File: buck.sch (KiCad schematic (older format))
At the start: 12 parts, among them U5 MP1584EN

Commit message: Rename to Sailor Hat
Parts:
- U5: symbol pi-supercap-ups:MP1584EN -> sailor-hat-rescue:MP1584EN-sailor-hat
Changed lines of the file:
@@
-EESchema Schematic File Version 5
-LIBS:pi-supercap-ups-cache
+EESchema Schematic File Version 4
 EELAYER 30 0
 EELAYER END
@@
 Comment3 ""
 Comment4 ""
-Comment5 ""
-Comment6 ""
-Comment7 ""
-Comment8 ""
-Comment9 ""
 $EndDescr
 $Comp
-L pi-supercap-ups:MP1584EN U?
+L sailor-hat-rescue:MP1584EN-sailor-hat U?
 U 1 1 5CA62D44
 P 3050 2350

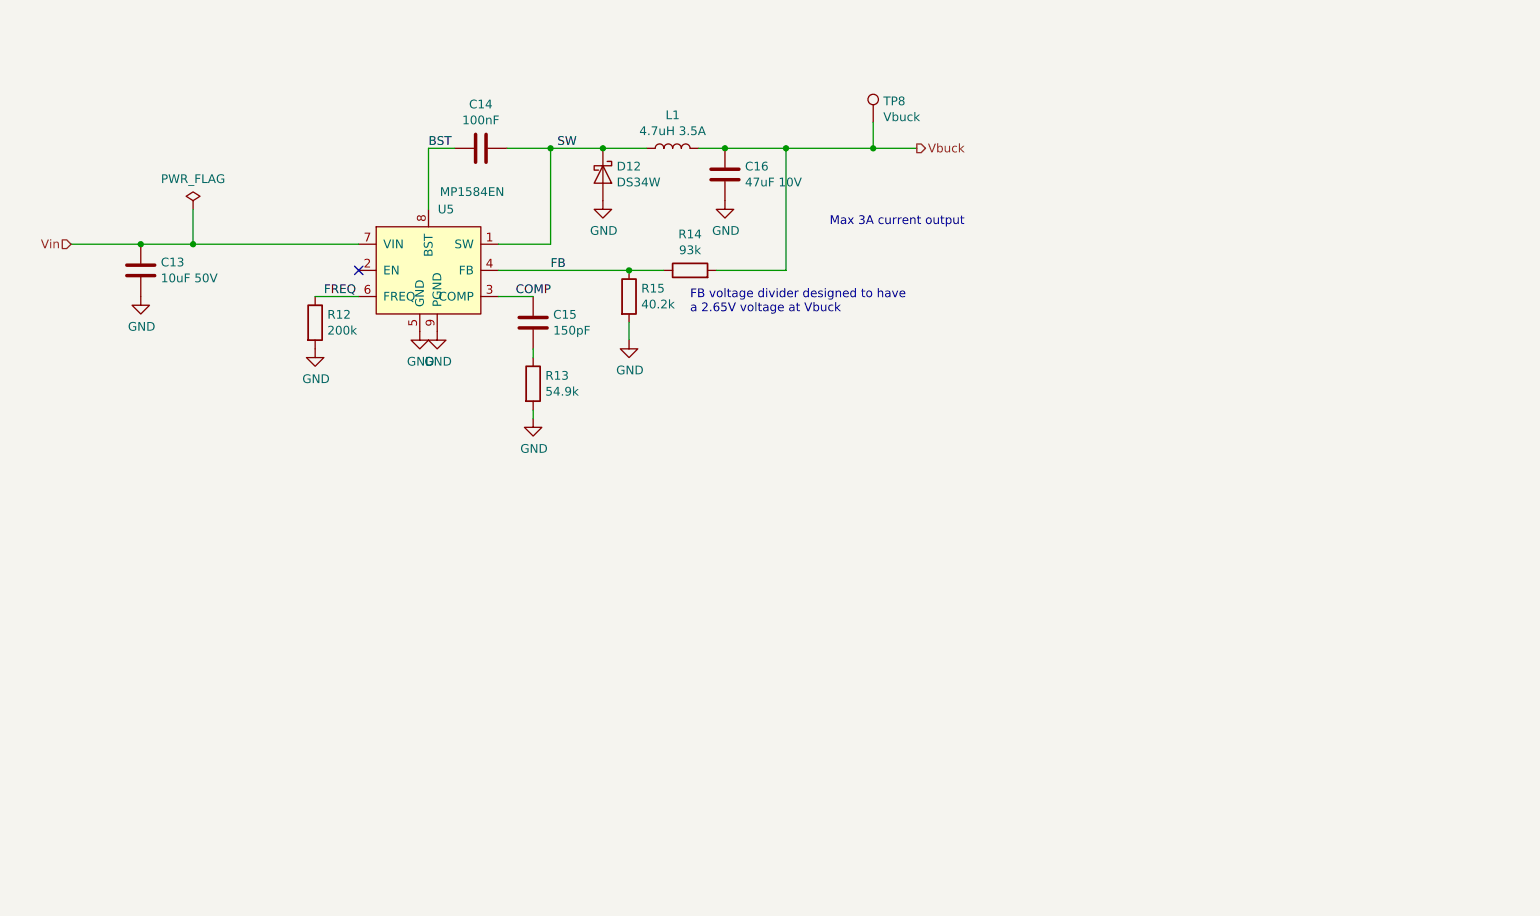
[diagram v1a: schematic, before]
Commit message: Implement better current limiting
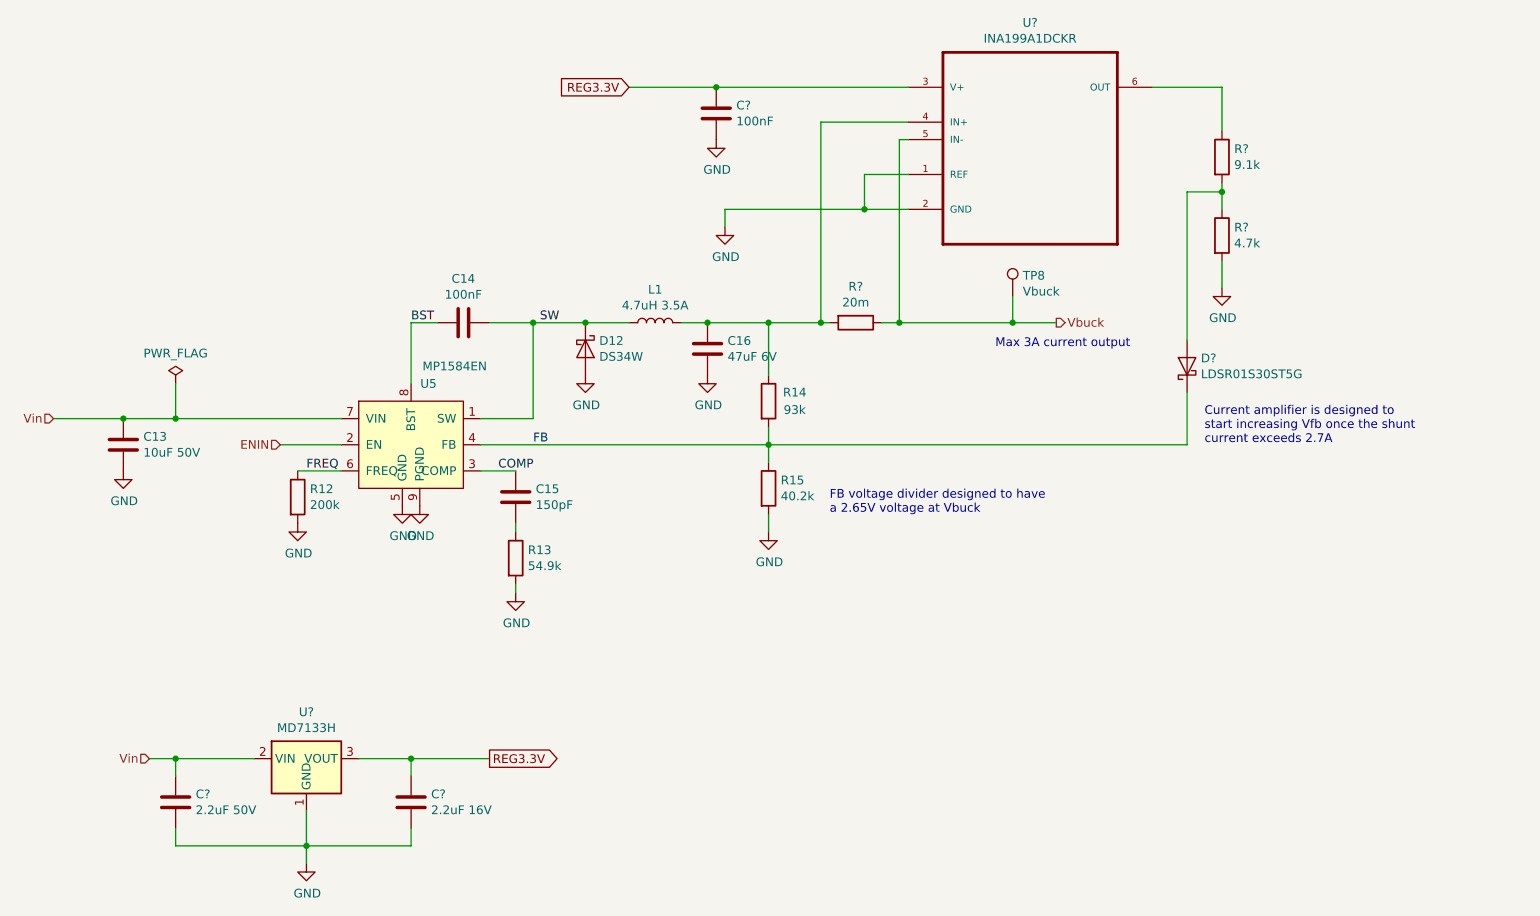
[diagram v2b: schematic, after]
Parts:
- added C?: 100nF, symbol Device:C
- added C?: 2.2uF 50V, symbol Device:C
- added C?: 2.2uF 16V, symbol Device:C
- added D?: LDSR01S30ST5G, symbol Device:D_Schottky
- added R?: 20m, symbol Device:R
- added R?: 9.1k, symbol Device:R
- added R?: 4.7k, symbol Device:R
- added U?: INA199A1DCKR, SOT65P210X110-6N, symbol sailor-hat:INA199A1DCKR
- added U?: MD7133H, Package_TO_SOT_SMD:SOT-89-3, symbol Regulator_Linear:HT75xx-1-SOT89
- C16: value 47uF 10V -> 47uF 6V
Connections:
- net FB: now also R14.2, D?.1 (K); no longer R14.1
- net GND: now also C?.2, C?.2, C?.2, R?.2, U?.1 (GND), U?.1 (REF), U?.2 (GND)
- net Vbuck: now also R?.1, U?.5 (IN-); no longer C16.1, L1.2, R14.2
- net Vin: now also C?.1, U?.2 (VIN)
- net ENIN: now reaches U5.2 (EN)
- new net: C16.1, L1.2, R14.1, R?.2, U?.4 (IN+)
- new net: R?.1, U?.6 (OUT)
- new net: D?.2 (A), R?.1, R?.2
- new net REG3.3V: C?.1, C?.1, U?.3 (V+), U?.3 (VOUT)
- no-connect marks 1 -> 0
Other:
- note added: "Current amplifier is designed to\nstart increasing Vfb once the shunt\ncurrent exceeds 2.7A"
- moved on the sheet: C13, C14, C15, C16, D12, L1, R12, R13, R14, R15, TP8, U5

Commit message: Add test points for new features
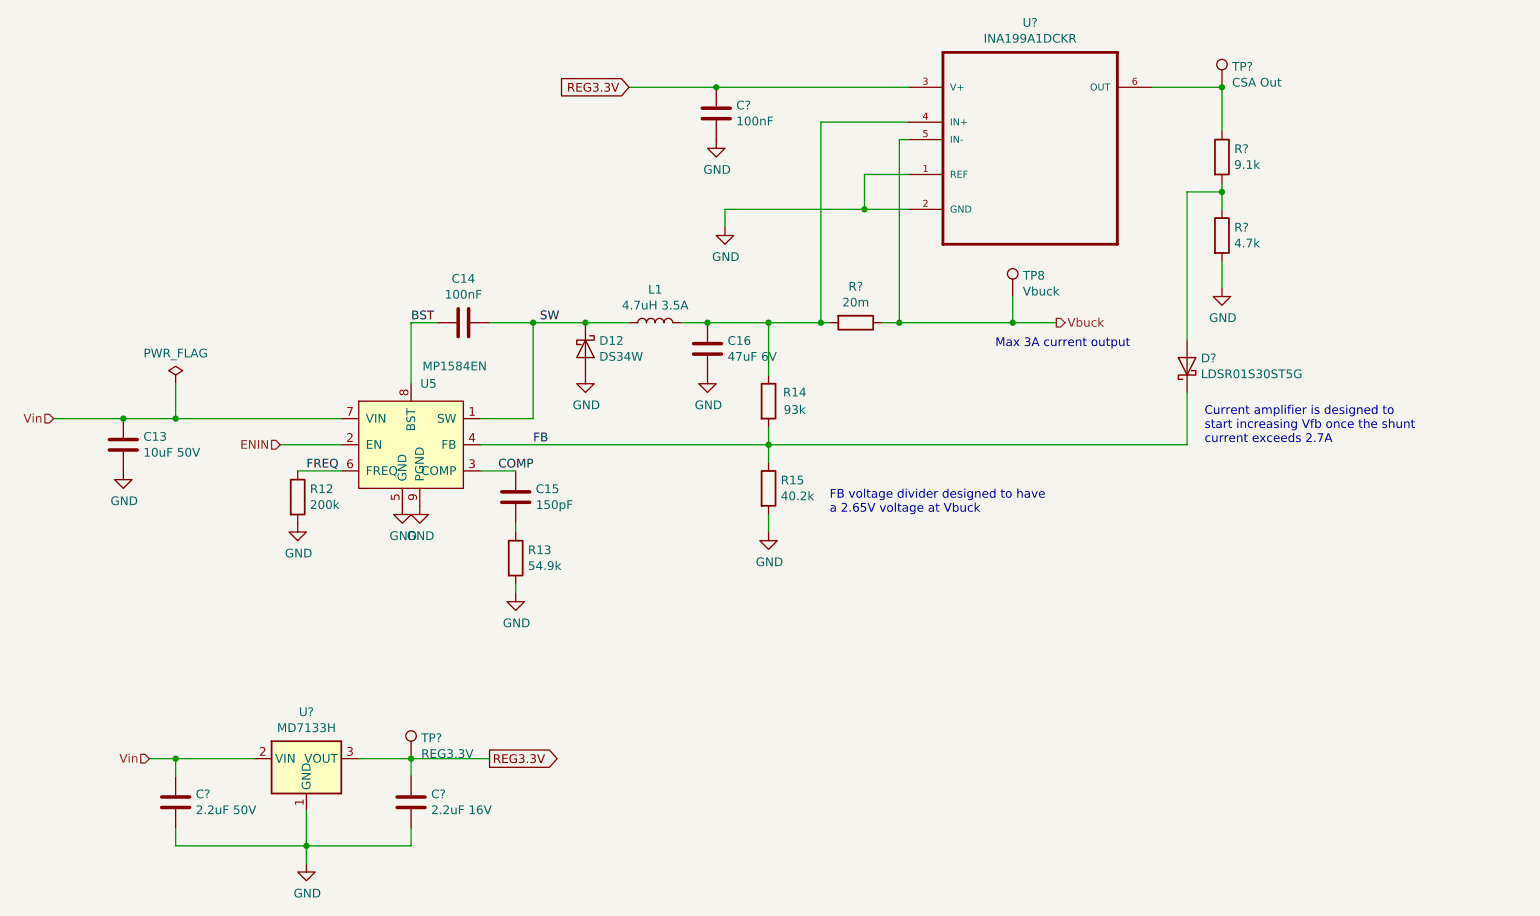
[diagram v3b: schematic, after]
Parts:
- added TP?: CSA Out, symbol Connector:TestPoint
- added TP?: REG3.3V, symbol Connector:TestPoint
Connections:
- net REG3.3V: now also TP?.1
- net at R?.1, U?.6 (OUT): now also TP?.1
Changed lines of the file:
@@
 Wire Wire Line
 	2200 3350 2550 3350
+$Comp
+L Connector:TestPoint TP?
+U 1 1 5E2A7700
+P 7600 1300
+F 0 "TP?" H 7658 1418 50  0000 L CNN
+F 1 "CSA Out" H 7658 1327 50  0000 L CNN
+F 2 "" H 7800 1300 50  0001 C CNN
+F 3 "~" H 7800 1300 50  0001 C CNN
+	1    7600 1300
+	1    0    0    -1
+$EndComp
+Connection ~ 7600 1300
+$Comp
+L Connector:TestPoint TP?
+U 1 1 5E2A8B09
+P 2950 5150
+F 0 "TP?" H 3008 5268 50  0000 L CNN
+F 1 "REG3.3V" H 3008 5177 50  0000 L CNN
+F 2 "" H 3150 5150 50  0001 C CNN
+F 3 "~" H 3150 5150 50  0001 C CNN
+	1    2950 5150
+	1    0    0    -1
+$EndComp
 $EndSCHEMATC

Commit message: Annotate and tweak power flags
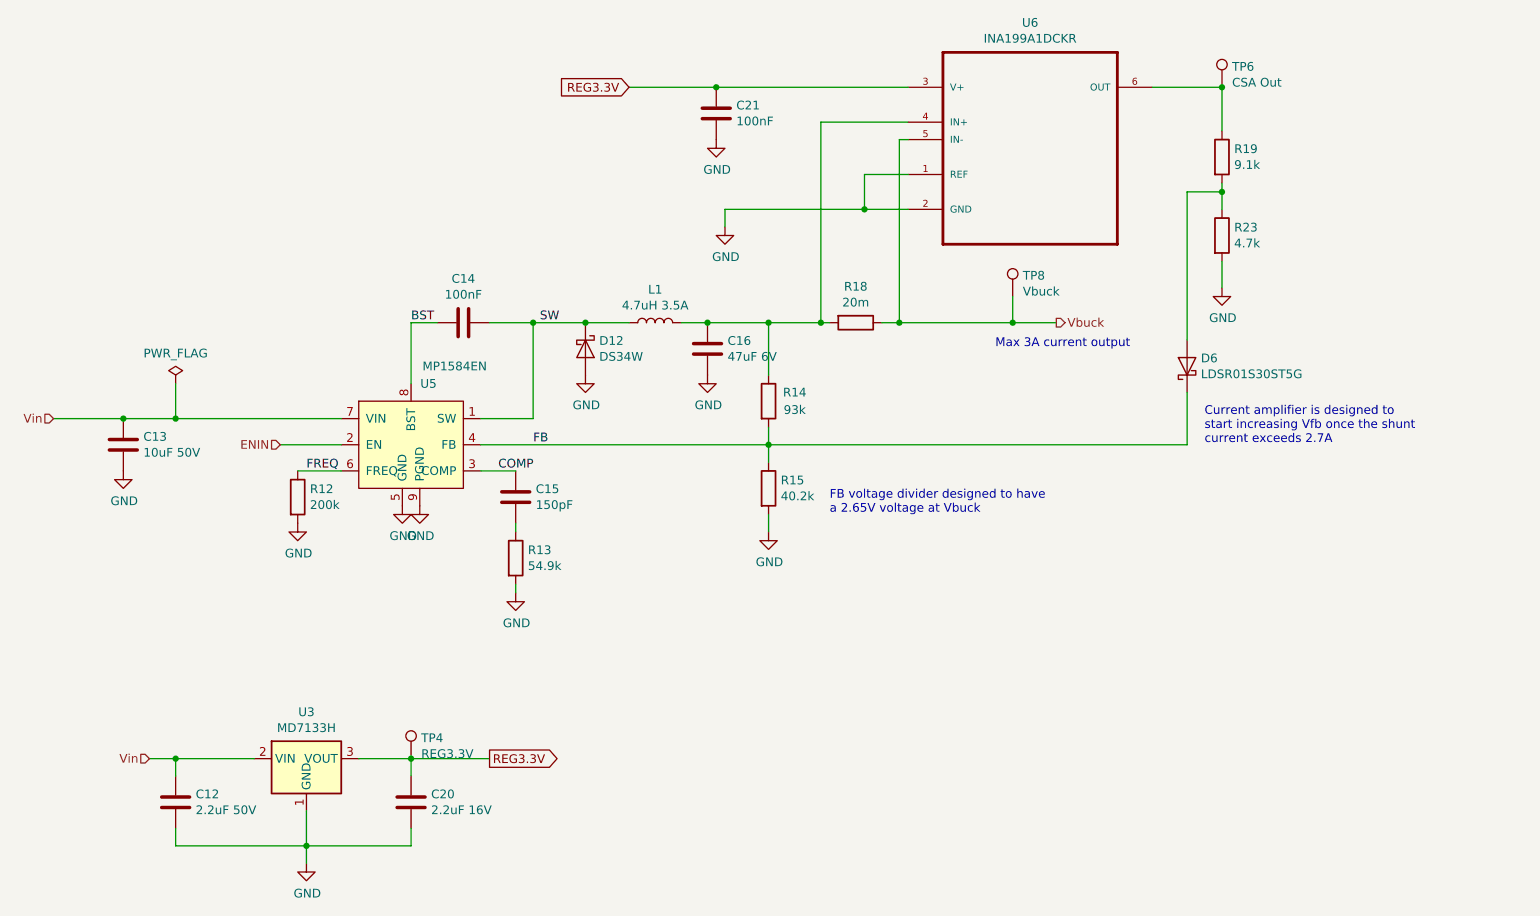
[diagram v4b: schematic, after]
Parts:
- gave numbers to parts that had none: 11
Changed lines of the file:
@@
 Connection ~ 5000 3350
 $Comp
-L sailor-hat:INA199A1DCKR U?
+L sailor-hat:INA199A1DCKR U6
 U 1 1 5E255BE6
 P 6500 1500
-F 0 "U?" H 6500 2070 50  0000 C CNN
+F 0 "U6" H 6500 2070 50  0000 C CNN
 F 1 "INA199A1DCKR" H 6500 1979 50  0000 C CNN
 F 2 "SOT65P210X110-6N" H 6500 1500 50  0001 L BNN
@@
 AR Path="/5E266404" Ref="#PWR?"  Part="1"
 AR Path="/5C3476D8/5E266404" Ref="#PWR?"  Part="1"
-AR Path="/5CA65CC5/5E266404" Ref="#PWR?"  Part="1"
-F 0 "#PWR?" H 4750 1850 50  0001 C CNN
+AR Path="/5CA65CC5/5E266404" Ref="#PWR052"  Part="1"
+F 0 "#PWR052" H 4750 1850 50  0001 C CNN
 F 1 "GND" H 4755 1927 50  0000 C CNN
 F 2 "" H 4750 2100 50  0001 C CNN
@@
 	4750 2000 5550 2000
 $Comp
-L Device:C C?
+L Device:C C21
 U 1 1 5E2673D4
 P 4700 1450
-F 0 "C?" H 4815 1496 50  0000 L CNN
+F 0 "C21" H 4815 1496 50  0000 L CNN
 F 1 "100nF" H 4815 1405 50  0000 L CNN
 F 2 "" H 4738 1300 50  0001 C CNN
@@
 AR Path="/5E268125" Ref="#PWR?"  Part="1"
 AR Path="/5C3476D8/5E268125" Ref="#PWR?"  Part="1"
-AR Path="/5CA65CC5/5E268125" Ref="#PWR?"  Part="1"
-F 0 "#PWR?" H 4700 1350 50  0001 C CNN
+AR Path="/5CA65CC5/5E268125" Ref="#PWR051"  Part="1"
+F 0 "#PWR051" H 4700 1350 50  0001 C CNN
 F 1 "GND" H 4705 1427 50  0000 C CNN
 F 2 "" H 4700 1600 50  0001 C CNN
@@
 	5550 2000 5800 2000
 $Comp
-L Device:R R?
+L Device:R R18
 U 1 1 5E26BA09
 P 5500 2650
-F 0 "R?" V 5293 2650 50  0000 C CNN
+F 0 "R18" V 5293 2650 50  0000 C CNN
 F 1 "20m" V 5384 2650 50  0000 C CNN
 F 2 "" V 5430 2650 50  0001 C CNN
@@
 	7400 3350 5000 3350
 $Comp
-L Device:R R?
+L Device:R R19
 U 1 1 5E26E2D4
 P 7600 1700
-F 0 "R?" H 7670 1746 50  0000 L CNN
+F 0 "R19" H 7670 1746 50  0000 L CNN
 F 1 "9.1k" H 7670 1655 50  0000 L CNN
 F 2 "" V 7530 1700 50  0001 C CNN
@@
 $EndComp
 $Comp
-L Device:R R?
+L Device:R R23
 U 1 1 5E2701E7
 P 7600 2150
-F 0 "R?" H 7670 2196 50  0000 L CNN
+F 0 "R23" H 7670 2196 50  0000 L CNN
 F 1 "4.7k" H 7670 2105 50  0000 L CNN
 F 2 "" V 7530 2150 50  0001 C CNN
@@
 $EndComp
 $Comp
-L Device:D_Schottky D?
+L Device:D_Schottky D6
 U 1 1 5E271FB2
 P 7400 2900
-F 0 "D?" V 7446 2821 50  0000 R CNN
+F 0 "D6" V 7446 2821 50  0000 R CNN
 F 1 "LDSR01S30ST5G" V 7355 2821 50  0000 R CNN
 F 2 "" H 7400 2900 50  0001 C CNN
@@
 AR Path="/5E27269A" Ref="#PWR?"  Part="1"
 AR Path="/5C3476D8/5E27269A" Ref="#PWR?"  Part="1"
-AR Path="/5CA65CC5/5E27269A" Ref="#PWR?"  Part="1"
-F 0 "#PWR?" H 7600 2200 50  0001 C CNN
+AR Path="/5CA65CC5/5E27269A" Ref="#PWR053"  Part="1"
+F 0 "#PWR053" H 7600 2200 50  0001 C CNN
 F 1 "GND" H 7605 2277 50  0000 C CNN
 F 2 "" H 7600 2450 50  0001 C CNN
@@
 	4700 1300 5800 1300
 $Comp
-L Regulator_Linear:HT75xx-1-SOT89 U?
+L Regulator_Linear:HT75xx-1-SOT89 U3
 U 1 1 5E27841B
 P 2350 5250
-F 0 "U?" H 2350 5617 50  0000 C CNN
+F 0 "U3" H 2350 5617 50  0000 C CNN
 F 1 "MD7133H" H 2350 5526 50  0000 C CNN
 F 2 "Package_TO_SOT_SMD:SOT-89-3" H 2350 5575 50  0001 C CIN
@@
 $EndComp
 $Comp
-L Device:C C?
+L Device:C C12
 U 1 1 5E278894
 P 1600 5400
-F 0 "C?" H 1715 5446 50  0000 L CNN
+F 0 "C12" H 1715 5446 50  0000 L CNN
 F 1 "2.2uF 50V" H 1715 5355 50  0000 L CNN
 F 2 "" H 1638 5250 50  0001 C CNN
@@
 $EndComp
 $Comp
-L Device:C C?
+L Device:C C20
 U 1 1 5E278F8C
 P 2950 5400
-F 0 "C?" H 3065 5446 50  0000 L CNN
+F 0 "C20" H 3065 5446 50  0000 L CNN
 F 1 "2.2uF 16V" H 3065 5355 50  0000 L CNN
 F 2 "" H 2988 5250 50  0001 C CNN
@@
 	2350 5750 2350 5650
 $Comp
-L power:GND #PWR?
+L power:GND #PWR048
 U 1 1 5E27DCC7
 P 2350 5750
-F 0 "#PWR?" H 2350 5500 50  0001 C CNN
+F 0 "#PWR048" H 2350 5500 50  0001 C CNN
 F 1 "GND" H 2355 5577 50  0000 C CNN
 F 2 "" H 2350 5750 50  0001 C CNN
@@
 	2200 3350 2550 3350
 $Comp
-L Connector:TestPoint TP?
+L Connector:TestPoint TP6
 U 1 1 5E2A7700
 P 7600 1300
-F 0 "TP?" H 7658 1418 50  0000 L CNN
+F 0 "TP6" H 7658 1418 50  0000 L CNN
 F 1 "CSA Out" H 7658 1327 50  0000 L CNN
 F 2 "" H 7800 1300 50  0001 C CNN
@@
 Connection ~ 7600 1300
 $Comp
-L Connector:TestPoint TP?
+L Connector:TestPoint TP4
 U 1 1 5E2A8B09
 P 2950 5150
-F 0 "TP?" H 3008 5268 50  0000 L CNN
+F 0 "TP4" H 3008 5268 50  0000 L CNN
 F 1 "REG3.3V" H 3008 5177 50  0000 L CNN
 F 2 "" H 3150 5150 50  0001 C CNN
